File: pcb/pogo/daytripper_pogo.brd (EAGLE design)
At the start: 24 x 24 mm, 4 parts

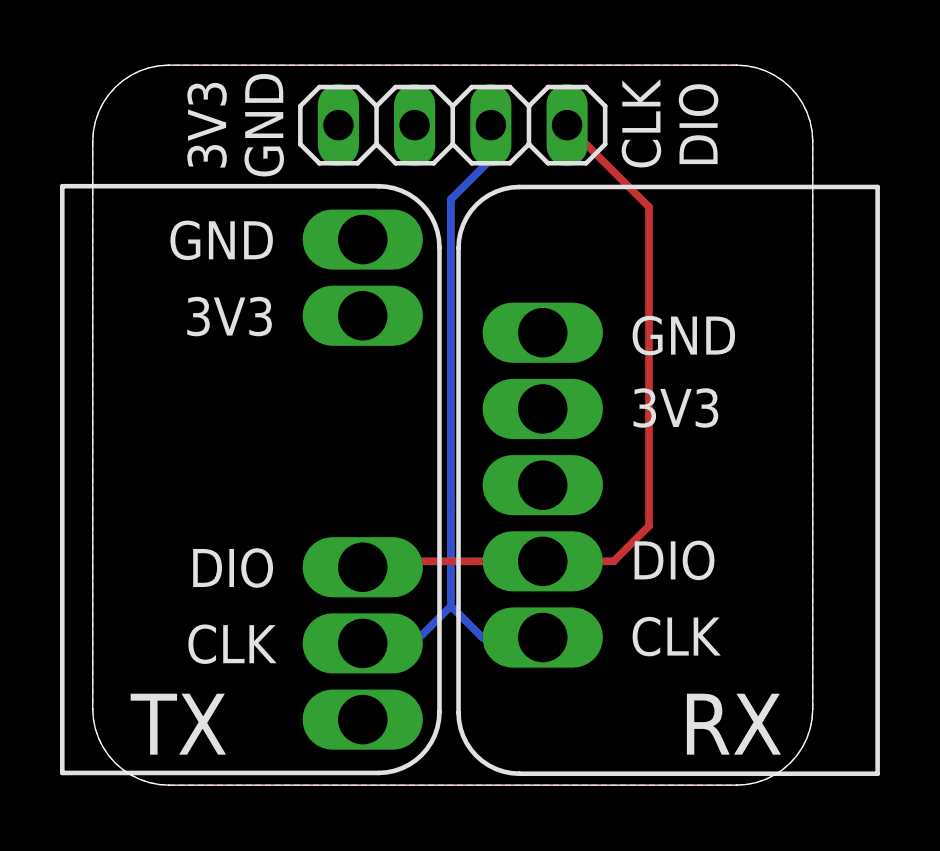
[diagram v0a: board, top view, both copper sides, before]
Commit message: redesigned pogo board
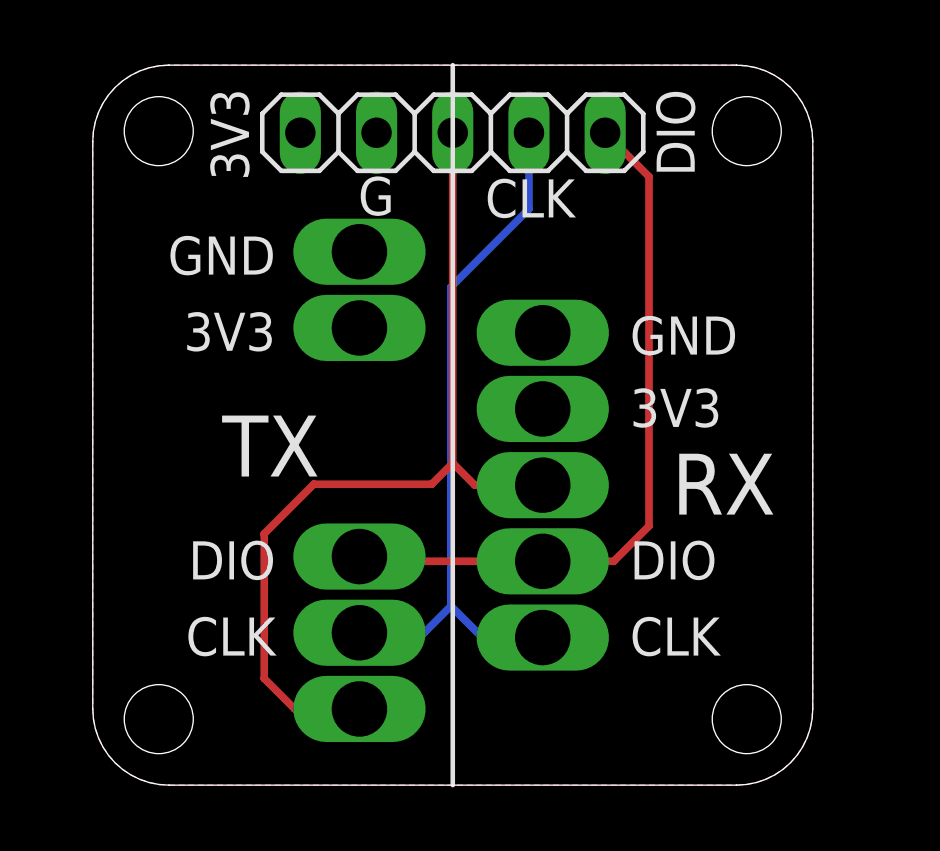
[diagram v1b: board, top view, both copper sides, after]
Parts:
- added U$12, U$13, U$14, U$4: M2_SCREW_DEV, 3pos_slide_switch:M2_SCREW_FOOT
- JP1: device pinhead:1X04 -> pinhead:1X05
- moved U$1 0.42 mm to (8.89, 16.5)
- moved U$2 0.37 mm to (8.89, 5.08)
- moved JP1 0.25 mm to (12.0, 21.7)
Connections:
- new net N$1: JP1.3, U$2.1, U$3.3
- net CLK: now also JP1.4; no longer JP1.3
- net DIO: now also JP1.5; no longer JP1.4
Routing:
- net N$1: track 0.00 -> 30.0 mm
- net DIO: track 24.6 -> 23.9 mm
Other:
- board text added: "G"
- board text added: "dayTripper Pogo"
- board text added: "dekuNukem 2019"
- board text removed: "dayTripper Pogo dekuNukem 2018"
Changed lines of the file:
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@@
 <setting verticaltext="up"/>
 </settings>
-<grid distance="5" unitdist="mil" unit="mil" style="lines" multiple="1" display="no" altdistance="5" altunitdist="mil" altunit="mil"/>
+<grid distance="5" unitdist="mil" unit="mil" style="lines" multiple="1" display="no" altdistance="1" altunitdist="mil" altunit="mil"/>
 <layers>
 <layer number="1" name="Top" color="4" fill="1" visible="yes" active="yes"/>
@@
 <wire x1="21.46" y1="24" x2="2.54" y2="24" width="0" layer="20"/>
 <wire x1="2.54" y1="24" x2="0" y2="21.46" width="0" layer="20" curve="90"/>
-<wire x1="-1.016" y1="19.9644" x2="9.525" y2="19.9644" width="0.1524" layer="25"/>
-<wire x1="9.525" y1="19.9644" x2="11.557" y2="17.9324" width="0.1524" layer="25" curve="-90"/>
-<wire x1="11.557" y1="17.9324" x2="11.557" y2="2.4384" width="0.1524" layer="25"/>
-<wire x1="11.557" y1="2.4384" x2="9.525" y2="0.4064" width="0.1524" layer="25" curve="-90"/>
-<wire x1="9.525" y1="0.4064" x2="-1.016" y2="0.4064" width="0.1524" layer="25"/>
-<wire x1="-1.016" y1="0.4064" x2="-1.016" y2="19.9644" width="0.1524" layer="25"/>
-<wire x1="26.162" y1="19.939" x2="14.224" y2="19.939" width="0.1524" layer="25"/>
-<wire x1="14.224" y1="19.939" x2="12.192" y2="17.907" width="0.1524" layer="25" curve="90"/>
-<wire x1="12.192" y1="17.907" x2="12.192" y2="2.413" width="0.1524" layer="25"/>
-<wire x1="12.192" y1="2.413" x2="14.224" y2="0.381" width="0.1524" layer="25" curve="90"/>
-<wire x1="14.224" y1="0.381" x2="26.162" y2="0.381" width="0.1524" layer="25"/>
-<wire x1="26.162" y1="0.381" x2="26.162" y2="19.939" width="0.1524" layer="25"/>
-<text x="6.096" y="18.796" size="1.27" layer="25" rot="R180">GND</text>
-<text x="6.096" y="16.256" size="1.27" layer="25" rot="R180">3V3</text>
-<text x="6.096" y="7.874" size="1.27" layer="25" rot="R180">DIO</text>
-<text x="6.096" y="5.334" size="1.27" layer="25" rot="R180">CLK</text>
+<wire x1="12" y1="24" x2="12" y2="0" width="0.1524" layer="25"/>
+<text x="6.096" y="18.288" size="1.27" layer="25" rot="R180">GND</text>
+<text x="6.096" y="15.748" size="1.27" layer="25" rot="R180">3V3</text>
+<text x="6.096" y="8.128" size="1.27" layer="25" rot="R180">DIO</text>
+<text x="6.096" y="5.588" size="1.27" layer="25" rot="R180">CLK</text>
 <text x="17.907" y="4.318" size="1.27" layer="25">CLK</text>
 <text x="17.907" y="6.858" size="1.27" layer="25">DIO</text>
 <text x="17.907" y="11.938" size="1.27" layer="25">3V3</text>
 <text x="17.907" y="14.351" size="1.27" layer="25">GND</text>
-<text x="1.27" y="1.016" size="2.032" layer="25">TX</text>
-<text x="19.558" y="1.016" size="2.032" layer="25">RX</text>
-<text x="3.81" y="22" size="1.27" layer="25" rot="R270" align="center">3V3</text>
-<text x="5.715" y="22" size="1.27" layer="25" rot="R270" align="center">GND</text>
-<text x="18.288" y="22" size="1.27" layer="25" rot="R270" align="center">CLK</text>
-<text x="20.193" y="22" size="1.27" layer="25" rot="R270" align="center">DIO</text>
-<text x="3.5" y="12" size="1.27" layer="26" rot="MR90" align="center">dayTripper Pogo
-dekuNukem 2018</text>
+<text x="4.318" y="10.287" size="2.032" layer="25">TX</text>
+<text x="19.304" y="9.017" size="2.032" layer="25">RX</text>
+<text x="4.572" y="21.688" size="1.27" layer="25" rot="R90" align="center">3V3</text>
+<text x="9.4524" y="19.6342" size="1.27" layer="25" align="center">G</text>
+<text x="14.576" y="19.558" size="1.27" layer="25" align="center">CLK</text>
+<text x="19.431" y="21.746" size="1.27" layer="25" rot="R270" align="center">DIO</text>
+<text x="2.5" y="12" size="1.27" layer="26" rot="MR90" align="center">dekuNukem 2019</text>
+<text x="22" y="12" size="1.27" layer="26" rot="MR90" align="center">dayTripper Pogo</text>
 </plain>
 <attributes>
@@
 </autorouter>
 <elements>
-<element name="U$1" library="3pos_slide_switch" package="1X02" value="POGO-1X2" x="9" y="16.9164" smashed="yes" rot="R90"/>
-<element name="U$2" library="3pos_slide_switch" package="1X03" value="POGO-1X3" x="9" y="4.7244" smashed="yes" rot="R90"/>
+<element name="U$1" library="3pos_slide_switch" package="1X02" value="POGO-1X2" x="8.89" y="16.51" smashed="yes" rot="R90"/>
+<element name="U$2" library="3pos_slide_switch" package="1X03" value="POGO-1X3" x="8.89" y="5.08" smashed="yes" rot="R90"/>
 <element name="U$3" library="3pos_slide_switch" package="1X05" value="POGO-1X5" x="15" y="10" smashed="yes" rot="R270"/>
-<element name="JP1" library="pinhead" library_urn="urn:adsk.eagle:library:325" package="1X04" package3d_urn="urn:adsk.eagle:package:22407/2" value="" x="12" y="22" smashed="yes">
-<attribute name="VALUE" x="6.92" y="18.825" size="1.27" layer="27"/>
+<element name="JP1" library="pinhead" library_urn="urn:adsk.eagle:library:325" package="1X05" package3d_urn="urn:adsk.eagle:package:22469/2" value="" x="12" y="21.746" smashed="yes">
+<attribute name="VALUE" x="6.92" y="18.571" size="1.27" layer="27"/>
 </element>
+<element name="U$4" library="3pos_slide_switch" package="M2_SCREW_FOOT" value="M2_SCREW_DEV" x="2.2" y="2.2"/>
+<element name="U$12" library="3pos_slide_switch" package="M2_SCREW_FOOT" value="M2_SCREW_DEV" x="2.2" y="21.8"/>
+<element name="U$13" library="3pos_slide_switch" package="M2_SCREW_FOOT" value="M2_SCREW_DEV" x="21.8" y="2.2"/>
+<element name="U$14" library="3pos_slide_switch" package="M2_SCREW_FOOT" value="M2_SCREW_DEV" x="21.8" y="21.8"/>
 </elements>
 <signals>
@@
 </signal>
 <signal name="CLK">
-<contactref element="JP1" pad="3"/>
-<contactref element="U$2" pad="2"/>
-<wire x1="13.27" y1="20.857" x2="11.938" y2="19.525" width="0.254" layer="16"/>
-<wire x1="11.938" y1="19.525" x2="11.938" y2="9.144" width="0.254" layer="16"/>
+<wire x1="11.938" y1="16.604" x2="11.938" y2="9.144" width="0.254" layer="16"/>
 <wire x1="11.938" y1="9.144" x2="11.938" y2="5.969" width="0.254" layer="16"/>
-<wire x1="10.6934" y1="4.7244" x2="9" y2="4.7244" width="0.254" layer="16"/>
-<wire x1="11.938" y1="5.969" x2="10.6934" y2="4.7244" width="0.254" layer="16"/>
-<wire x1="13.27" y1="22" x2="13.27" y2="20.857" width="0.254" layer="16"/>
 <contactref element="U$3" pad="5"/>
 <wire x1="11.938" y1="5.969" x2="12.987" y2="4.92" width="0.254" layer="16"/>
 <wire x1="12.987" y1="4.92" x2="15" y2="4.92" width="0.254" layer="16"/>
+<contactref element="U$2" pad="2"/>
+<contactref element="JP1" pad="4"/>
+<wire x1="14.54" y1="21.746" x2="14.54" y2="19.206" width="0.254" layer="16"/>
+<wire x1="14.54" y1="19.206" x2="11.938" y2="16.604" width="0.254" layer="16"/>
+<wire x1="11.049" y1="5.08" x2="8.89" y2="5.08" width="0.254" layer="16"/>
+<wire x1="11.938" y1="5.969" x2="11.049" y2="5.08" width="0.254" layer="16"/>
 </signal>
 <signal name="DIO">
-<contactref element="JP1" pad="4"/>
+<contactref element="U$3" pad="4"/>
+<wire x1="17.366" y1="7.46" x2="18.542" y2="8.636" width="0.254" layer="1"/>
+<wire x1="17.366" y1="7.46" x2="15" y2="7.46" width="0.254" layer="1"/>
+<wire x1="9.1956" y1="7.46" x2="15" y2="7.46" width="0.254" layer="1"/>
 <contactref element="U$2" pad="3"/>
-<contactref element="U$3" pad="4"/>
-<wire x1="15.81" y1="22" x2="18.542" y2="19.268" width="0.254" layer="1"/>
-<wire x1="18.542" y1="19.268" x2="18.542" y2="8.636" width="0.254" layer="1"/>
-<wire x1="18.542" y1="8.636" x2="17.366" y2="7.46" width="0.254" layer="1"/>
-<wire x1="17.366" y1="7.46" x2="15" y2="7.46" width="0.254" layer="1"/>
-<wire x1="15" y1="7.46" x2="9.1956" y2="7.46" width="0.254" layer="1"/>
-<wire x1="9.1956" y1="7.46" x2="9" y2="7.2644" width="0.254" layer="1"/>
+<contactref element="JP1" pad="5"/>
+<wire x1="18.542" y1="20.284" x2="17.08" y2="21.746" width="0.254" layer="1"/>
+<wire x1="18.542" y1="8.636" x2="18.542" y2="20.284" width="0.254" layer="1"/>
+<wire x1="8.89" y1="7.62" x2="9.0356" y2="7.62" width="0.254" layer="1"/>
+<wire x1="9.0356" y1="7.62" x2="9.1956" y2="7.46" width="0.254" layer="1"/>
+</signal>
+<signal name="N$1">
+<contactref element="U$2" pad="1"/>
+<contactref element="JP1" pad="3"/>
+<contactref element="U$3" pad="3"/>
+<wire x1="12" y1="21.746" x2="12" y2="10.733" width="0.254" layer="1"/>
+<wire x1="8.89" y1="2.54" x2="6.731" y2="2.54" width="0.254" layer="1"/>
+<wire x1="5.715" y1="3.556" x2="6.731" y2="2.54" width="0.254" layer="1"/>
+<wire x1="12" y1="10.733" x2="11.3" y2="10.033" width="0.254" layer="1"/>
+<wire x1="11.3" y1="10.033" x2="7.366" y2="10.033" width="0.254" layer="1"/>
+<wire x1="7.366" y1="10.033" x2="5.715" y2="8.382" width="0.254" layer="1"/>
+<wire x1="5.715" y1="8.382" x2="5.715" y2="3.556" width="0.254" layer="1"/>
+<wire x1="15" y1="10" x2="12.733" y2="10" width="0.254" layer="1"/>
+<wire x1="12.733" y1="10" x2="12" y2="10.733" width="0.254" layer="1"/>
 </signal>
 </signals>
@@
 </drawing>
 <compatibility>
-<note version="6.3" minversion="6.2.2" severity="warning">
-Since Version 6.2.2 text objects can contain more than one line,
-which will not be processed correctly with this version.
-</note>
 <note version="8.2" severity="warning">
 Since Version 8.2, EAGLE supports online libraries. The ids
